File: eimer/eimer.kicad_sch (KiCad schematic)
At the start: 33 parts, among them J1 Conn_01x20, J2 Conn_01x20, J3 Conn_01x03, J4 USB_C_Receptacle_USB2.0_14P, SW1 SW_Push, U1 RP2040, U2 NCP1117-3.3_SOT223, U3 W25Q128JVS, Y1 12 MHz

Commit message: started layout of pcb
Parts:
- removed U2: NCP1117-3.3_SOT223, Package_TO_SOT_SMD:SOT-223-3_TabPin2, symbol Regulator_Linear:NCP1117-3.3_SOT223
- removed U3: W25Q128JVS, Package_SO:SOIC-8_5.3x5.3mm_P1.27mm, symbol Memory_Flash:W25Q128JVS
- added U2: MCP1700x-330xxTT, Package_TO_SOT_SMD:SOT-23, symbol Regulator_Linear:MCP1700x-330xxTT
- added U4: W25Q16JVUXIQ TR, Package_SON:Winbond_USON-8-1EP_3x2mm_P0.5mm_EP0.2x1.6mm, symbol Memory_Flash:W25Q16JVSS
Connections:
- net +3.3V: now also U2.2 (VO), U4.8 (VCC)
- net GND: now also U2.1 (GND), U4.4 (GND)
- net QSPI_SCLK: now also U4.6 (CLK)
- net QSPI_SD0: now also U4.5 (DI/IO_{0})
- net QSPI_SD1: now also U4.2 (DO/IO_{1})
- net QSPI_SD2: now also U4.3 (~{WP}/IO_{2})
- net QSPI_SD3: now also U4.7 (~{HOLD}/~{RESET}/IO_{3})
- net QSPI_SS: now also U4.1 (~{CS})
- net VBUS: now also U2.3 (VI)
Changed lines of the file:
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@@
 	)
 	(symbol
+		(lib_id "Memory_Flash:W25Q16JVSS")
+		(at 226.06 124.46 0)
+		(unit 1)
+		(body_style 1)
+		(exclude_from_sim no)
+		(in_bom yes)
+		(on_board yes)
+		(in_pos_files yes)
+		(dnp no)
+		(fields_autoplaced yes)
+		(property "Reference" "U4"
+			(at 237.49 123.1899 0)
+			(show_name no)
+			(do_not_autoplace no)
+			(effects
+				(font
+					(size 1.27 1.27)
+				)
+				(justify left)
+			)
+		)
+		(property "Value" "W25Q16JVUXIQ TR"
+			(at 237.49 125.7299 0)
+			(show_name no)
+			(do_not_autoplace no)
+			(effects
+				(font
+					(size 1.27 1.27)
+				)
+				(justify left)
+			)
+		)
+		(property "Footprint" "Package_SON:Winbond_USON-8-1EP_3x2mm_P0.5mm_EP0.2x1.6mm"
+			(at 226.06 124.46 0)
+			(hide yes)
+			(show_name no)
+			(do_not_autoplace no)
+			(effects
+				(font
+					(size 1.27 1.27)
+				)
+			)
+		)
+		(property "Datasheet" ""
+			(at 226.06 124.46 0)
+			(hide yes)
+			(show_name no)
+			(do_not_autoplace no)
+			(effects
+				(font
+					(size 1.27 1.27)
+				)
+			)
+		)
+		(property "Description" ""
+			(at 226.06 124.46 0)
+			(hide yes)
+			(show_name no)
+			(do_not_autoplace no)
+			(effects
+				(font
+					(size 1.27 1.27)
+				)
+			)
+		)
+		(pin "5"
+		)
+		(pin "8"
+		)
+		(pin "4"
+		)
+		(pin "3"
+		)
+		(pin "2"
+		)
+		(pin "6"
+		)
+		(pin "1"
+		)
+		(pin "7"
+		)
+		(instances
+			(project "eimer"
+				(path "/310aac61-9967-4677-964a-8a6056e13ca2"
+					(reference "U4")
+					(unit 1)
+				)
+			)
+		)
+	)
+	(symbol
 		(lib_id "Connector_Generic:Conn_01x20")
 		(at 55.88 87.63 0)
@@
 	)
 	(symbol
+		(lib_id "Regulator_Linear:MCP1700x-330xxTT")
+		(at 248.92 33.02 0)
+		(unit 1)
+		(body_style 1)
+		(exclude_from_sim no)
+		(in_bom yes)
+		(on_board yes)
+		(in_pos_files yes)
+		(dnp no)
+		(fields_autoplaced yes)
+		(property "Reference" "U2"
+			(at 248.92 26.67 0)
+			(show_name no)
+			(do_not_autoplace no)
+			(effects
+				(font
+					(size 1.27 1.27)
+				)
+			)
+		)
+		(property "Value" "MCP1700x-330xxTT"
+			(at 248.92 29.21 0)
+			(show_name no)
+			(do_not_autoplace no)
+			(effects
+				(font
+					(size 1.27 1.27)
+				)
+			)
+		)
+		(property "Footprint" "Package_TO_SOT_SMD:SOT-23"
+			(at 248.92 27.305 0)
+			(hide yes)
+			(show_name no)
+			(do_not_autoplace no)
+			(effects
+				(font
+					(size 1.27 1.27)
+				)
+			)
+		)
+		(property "Datasheet" "http://ww1.microchip.com/downloads/en/DeviceDoc/20001826D.pdf"
+			(at 248.92 33.02 0)
+			(hide yes)
+			(show_name no)
+			(do_not_autoplace no)
+			(effects
+				(font
+					(size 1.27 1.27)
+				)
+			)
+		)
+		(property "Description" "250mA Low Quiscent Current LDO, 3.3V output, SOT-23"
+			(at 248.92 33.02 0)
+			(hide yes)
+			(show_name no)
+			(do_not_autoplace no)
+			(effects
+				(font
+					(size 1.27 1.27)
+				)
+			)
+		)
+		(pin "3"
+		)
+		(pin "2"
+		)
+		(pin "1"
+		)
+		(instances
+			(project "eimer"
+				(path "/310aac61-9967-4677-964a-8a6056e13ca2"
+					(reference "U2")
+					(unit 1)
+				)
+			)
+		)
+	)
+	(symbol
 		(lib_id "Connector:USB_C_Receptacle_USB2.0_14P")
 		(at 194.31 48.26 0)
@@
 	)
 	(symbol
-		(lib_id "Regulator_Linear:NCP1117-3.3_SOT223")
-		(at 248.92 33.02 0)
-		(unit 1)
-		(body_style 1)
-		(exclude_from_sim no)
-		(in_bom yes)
-		(on_board yes)
-		(in_pos_files yes)
-		(dnp no)
-		(fields_autoplaced yes)
-		(property "Reference" "U2"
-			(at 248.92 26.67 0)
-			(show_name no)
-			(do_not_autoplace no)
-			(effects
-				(font
-					(size 1.27 1.27)
-				)
-			)
-		)
-		(property "Value" "NCP1117-3.3_SOT223"
-			(at 248.92 29.21 0)
-			(show_name no)
-			(do_not_autoplace no)
-			(effects
-				(font
-					(size 1.27 1.27)
-				)
-			)
-		)
-		(property "Footprint" "Package_TO_SOT_SMD:SOT-223-3_TabPin2"
-			(at 248.92 27.94 0)
-			(hide yes)
-			(show_name no)
-			(do_not_autoplace no)
-			(effects
-				(font
-					(size 1.27 1.27)
-				)
-			)
-		)
-		(property "Datasheet" "http://www.onsemi.com/pub_link/Collateral/NCP1117-D.PDF"
-			(at 251.46 39.37 0)
-			(hide yes)
-			(show_name no)
-			(do_not_autoplace no)
-			(effects
-				(font
-					(size 1.27 1.27)
-				)
-			)
-		)
-		(property "Description" "1A Low drop-out regulator, Fixed Output 3.3V, SOT-223"
-			(at 248.92 33.02 0)
-			(hide yes)
-			(show_name no)
-			(do_not_autoplace no)
-			(effects
-				(font
-					(size 1.27 1.27)
-				)
-			)
-		)
-		(pin "2"
-		)
-		(pin "3"
-		)
-		(pin "1"
-		)
-		(instances
-			(project "eimer"
-				(path "/310aac61-9967-4677-964a-8a6056e13ca2"
-					(reference "U2")
-					(unit 1)
-				)
-			)
-		)
-	)
-	(symbol
 		(lib_id "Device:C")
 		(at 43.18 34.29 0)
@@
 					(unit 1)
 				)
-			)
-		)
-	)
-	(symbol
-		(lib_id "Memory_Flash:W25Q128JVS")
-		(at 226.06 124.46 0)
-		(unit 1)
-		(body_style 1)
-		(exclude_from_sim no)
-		(in_bom yes)
-		(on_board yes)
-		(in_pos_files yes)
-		(dnp no)
-		(fields_autoplaced yes)
-		(property "Reference" "U3"
-			(at 237.49 123.1899 0)
-			(show_name no)
-			(do_not_autoplace no)
-			(effects
-				(font
-					(size 1.27 1.27)
-				)
-				(justify left)
-			)
-		)
-		(property "Value" "W25Q128JVS"
-			(at 237.49 125.7299 0)
-			(show_name no)
-			(do_not_autoplace no)
-			(effects
-				(font
-					(size 1.27 1.27)
-				)
-				(justify left)
-			)
-		)
-		(property "Footprint" "Package_SO:SOIC-8_5.3x5.3mm_P1.27mm"
-			(at 226.06 101.6 0)
-			(hide yes)
-			(show_name no)
-			(do_not_autoplace no)
-			(effects
-				(font
-					(size 1.27 1.27)
-				)
-			)
-		)
-		(property "Datasheet" "https://www.winbond.com/resource-files/w25q128jv_dtr%20revc%2003272018%20plus.pdf"
-			(at 226.06 99.06 0)
-			(hide yes)
-			(show_name no)
-			(do_not_autoplace no)
-			(effects
-				(font
-					(size 1.27 1.27)
-				)
-			)
-		)
-		(property "Description" "128Mbit / 16MiB Serial Flash Memory, Standard/Dual/Quad SPI, 2.7-3.6V, SOIC-8"
-			(at 226.06 96.52 0)
-			(hide yes)
-			(show_name no)
-			(do_not_autoplace no)
-			(effects
-				(font
-					(size 1.27 1.27)
-				)
-			)
-		)
-		(pin "1"
-		)
-		(pin "2"
-		)
-		(pin "8"
-		)
-		(pin "5"
-		)
-		(pin "7"
-		)
-		(pin "6"
-		)
-		(pin "3"
-		)
-		(pin "4"
-		)
-		(instances
-			(project "eimer"
-				(path "/310aac61-9967-4677-964a-8a6056e13ca2"
-					(reference "U3")
-					(unit 1)
-				)

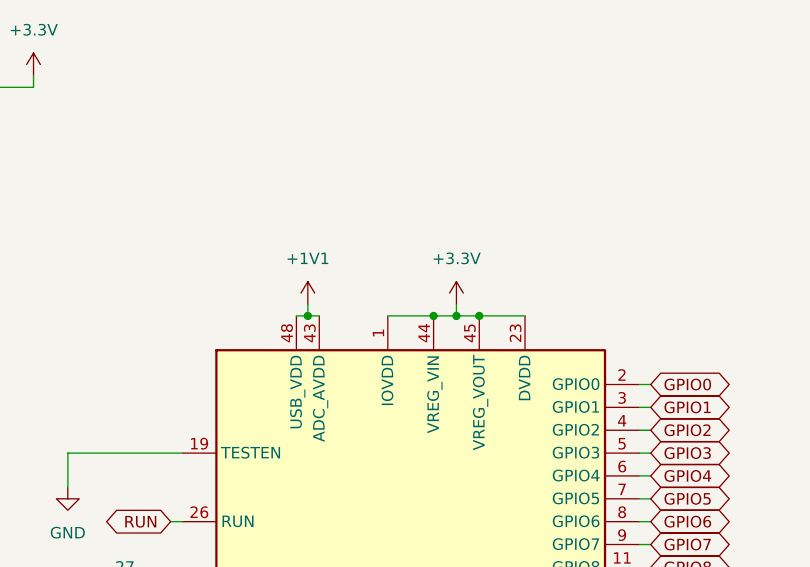
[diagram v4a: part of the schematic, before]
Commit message: fixed power nets
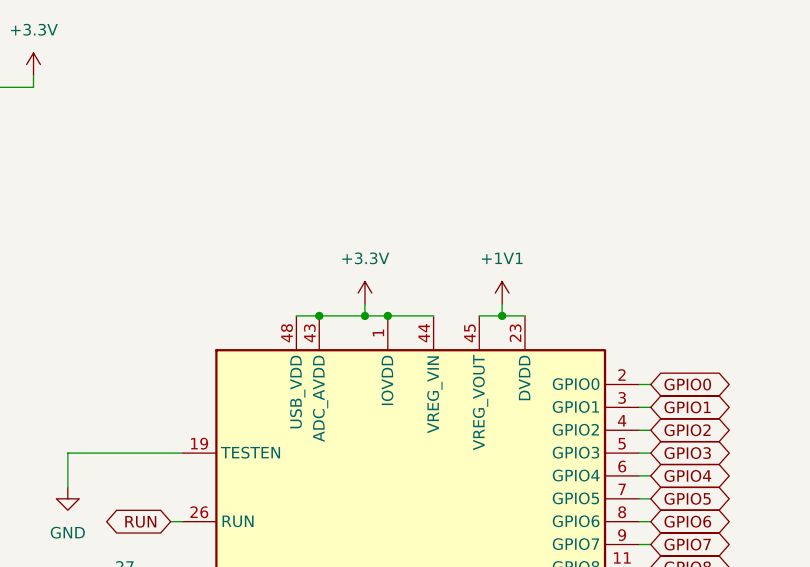
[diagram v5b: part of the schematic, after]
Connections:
- net +1V1: now also U1.23 (DVDD), U1.45 (VREG_VOUT), U1.50 (DVDD); no longer U1.43 (ADC_AVDD), U1.48 (USB_VDD)
- net +3.3V: now also U1.43 (ADC_AVDD), U1.48 (USB_VDD); no longer U1.23 (DVDD), U1.45 (VREG_VOUT), U1.50 (DVDD)
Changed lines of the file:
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@@
 	)
 	(junction
+		(at 120.65 100.33)
+		(diameter 0)
+		(color 0 0 0 0)
+	)
+	(junction
 		(at 110.49 30.48)
 		(diameter 0)
@@
 	)
 	(junction
-		(at 119.38 100.33)
-		(diameter 0)
-		(color 0 0 0 0)
-	)
-	(junction
 		(at 30.48 38.1)
 		(diameter 0)
@@
 	)
 	(junction
-		(at 138.43 100.33)
+		(at 123.19 30.48)
 		(diameter 0)
 		(color 0 0 0 0)
 	)
 	(junction
-		(at 123.19 30.48)
+		(at 85.09 38.1)
 		(diameter 0)
 		(color 0 0 0 0)
 	)
 	(junction
-		(at 85.09 38.1)
+		(at 97.79 30.48)
 		(diameter 0)
 		(color 0 0 0 0)
 	)
 	(junction
-		(at 97.79 30.48)
+		(at 140.97 100.33)
 		(diameter 0)
 		(color 0 0 0 0)
@@
 	)
 	(junction
-		(at 133.35 100.33)
+		(at 209.55 46.99)
 		(diameter 0)
 		(color 0 0 0 0)
 	)
 	(junction
-		(at 209.55 46.99)
+		(at 128.27 100.33)
 		(diameter 0)
 		(color 0 0 0 0)
@@
 	)
 	(junction
-		(at 226.06 109.22)
+		(at 125.73 100.33)
 		(diameter 0)
 		(color 0 0 0 0)
 	)
 	(junction
-		(at 135.89 100.33)
+		(at 226.06 109.22)
 		(diameter 0)
 		(color 0 0 0 0)
@@
 	(wire
 		(pts
-			(xy 133.35 100.33) (xy 135.89 100.33)
+			(xy 24.13 90.17) (xy 27.94 90.17)
 		)
 		(stroke
@@
 	(wire
 		(pts
-			(xy 24.13 90.17) (xy 27.94 90.17)
+			(xy 60.96 90.17) (xy 66.04 90.17)
 		)
 		(stroke
@@
 	(wire
 		(pts
-			(xy 60.96 90.17) (xy 66.04 90.17)
+			(xy 120.65 100.33) (xy 125.73 100.33)
 		)
 		(stroke
@@
 	(wire
 		(pts
-			(xy 118.11 100.33) (xy 119.38 100.33)
-		)
-		(stroke
-			(width 0)
-			(type default)
-		)
-	)
-	(wire
-		(pts
 			(xy 104.14 123.19) (xy 105.41 123.19)
 		)
@@
 	(wire
 		(pts
-			(xy 135.89 100.33) (xy 138.43 100.33)
-		)
-		(stroke
-			(width 0)
-			(type default)
-		)
-	)
-	(wire
-		(pts
 			(xy 156.21 184.15) (xy 157.48 184.15)
 		)
@@
 	(wire
 		(pts
+			(xy 140.97 99.06) (xy 140.97 100.33)
+		)
+		(stroke
+			(width 0)
+			(type default)
+		)
+	)
+	(wire
+		(pts
 			(xy 26.67 95.25) (xy 26.67 82.55)
 		)
@@
 	(wire
 		(pts
+			(xy 128.27 100.33) (xy 133.35 100.33)
+		)
+		(stroke
+			(width 0)
+			(type default)
+		)
+	)
+	(wire
+		(pts
 			(xy 233.68 40.64) (xy 248.92 40.64)
 		)
@@
 	(wire
 		(pts
+			(xy 125.73 99.06) (xy 125.73 100.33)
+		)
+		(stroke
+			(width 0)
+			(type default)
+		)
+	)
+	(wire
+		(pts
 			(xy 63.5 116.84) (xy 63.5 107.95)
 		)
@@
 	(wire
 		(pts
-			(xy 128.27 100.33) (xy 133.35 100.33)
-		)
-		(stroke
-			(width 0)
-			(type default)
-		)
-	)
-	(wire
-		(pts
-			(xy 119.38 100.33) (xy 120.65 100.33)
-		)
-		(stroke
-			(width 0)
-			(type default)
-		)
-	)
-	(wire
-		(pts
 			(xy 156.21 176.53) (xy 157.48 176.53)
 		)
@@
 	(wire
 		(pts
-			(xy 138.43 100.33) (xy 143.51 100.33)
-		)
-		(stroke
-			(width 0)
-			(type default)
-		)
-	)
-	(wire
-		(pts
 			(xy 201.93 114.3) (xy 201.93 116.84)
 		)
@@
 	(wire
 		(pts
-			(xy 135.89 99.06) (xy 135.89 100.33)
-		)
-		(stroke
-			(width 0)
-			(type default)
-		)
-	)
-	(wire
-		(pts
 			(xy 156.21 125.73) (xy 157.48 125.73)
 		)
@@
 	(wire
 		(pts
-			(xy 148.59 38.1) (xy 161.29 38.1)
+			(xy 140.97 100.33) (xy 143.51 100.33)
 		)
 		(stroke
@@
 	(wire
 		(pts
-			(xy 110.49 38.1) (xy 123.19 38.1)
+			(xy 148.59 38.1) (xy 161.29 38.1)
 		)
 		(stroke
@@
 	(wire
 		(pts
-			(xy 198.12 116.84) (xy 201.93 116.84)
+			(xy 110.49 38.1) (xy 123.19 38.1)
 		)
 		(stroke
@@
 	(wire
 		(pts
-			(xy 156.21 143.51) (xy 157.48 143.51)
+			(xy 198.12 116.84) (xy 201.93 116.84)
 		)
 		(stroke
@@
 	(wire
 		(pts
-			(xy 24.13 105.41) (xy 27.94 105.41)
+			(xy 156.21 143.51) (xy 157.48 143.51)
 		)
 		(stroke
@@
 	(wire
 		(pts
-			(xy 148.59 30.48) (xy 161.29 30.48)
+			(xy 24.13 105.41) (xy 27.94 105.41)
 		)
 		(stroke
@@
 	(wire
 		(pts
-			(xy 119.38 99.06) (xy 119.38 100.33)
+			(xy 148.59 30.48) (xy 161.29 30.48)
 		)
 		(stroke
@@
 	(wire
 		(pts
+			(xy 138.43 100.33) (xy 140.97 100.33)
+		)
+		(stroke
+			(width 0)
+			(type default)
+		)
+	)
+	(wire
+		(pts
 			(xy 256.54 33.02) (xy 262.89 33.02)
 		)
@@
 	(wire
 		(pts
+			(xy 125.73 100.33) (xy 128.27 100.33)
+		)
+		(stroke
+			(width 0)
+			(type default)
+		)
+	)
+	(wire
+		(pts
+			(xy 118.11 100.33) (xy 120.65 100.33)
+		)
+		(stroke
+			(width 0)
+			(type default)
+		)
+	)
+	(wire
+		(pts
 			(xy 40.64 121.92) (xy 41.91 121.92)
 		)
@@
 	(symbol
 		(lib_id "power:+3.3V")
-		(at 135.89 99.06 0)
+		(at 125.73 99.06 0)
 		(unit 1)
 		(body_style 1)
@@
 		(fields_autoplaced yes)
 		(property "Reference" "#PWR02"
-			(at 135.89 102.87 0)
+			(at 125.73 102.87 0)
 			(hide yes)
 			(show_name no)
@@
 		)
 		(property "Value" "+3.3V"
-			(at 135.89 93.98 0)
+			(at 125.73 93.98 0)
 			(show_name no)
 			(do_not_autoplace no)
@@
 		)
 		(property "Footprint" ""
-			(at 135.89 99.06 0)
+			(at 125.73 99.06 0)
 			(hide yes)
 			(show_name no)
@@
 		)
 		(property "Datasheet" ""
-			(at 135.89 99.06 0)
+			(at 125.73 99.06 0)
 			(hide yes)
 			(show_name no)
@@
 		)
 		(property "Description" "Power symbol creates a global label with name \"+3.3V\""
-			(at 135.89 99.06 0)
+			(at 125.73 99.06 0)
 			(hide yes)
 			(show_name no)
@@
 	(symbol
 		(lib_id "power:+1V1")
-		(at 119.38 99.06 0)
+		(at 140.97 99.06 0)
 		(unit 1)
 		(body_style 1)
@@
 		(fields_autoplaced yes)
 		(property "Reference" "#PWR01"
-			(at 119.38 102.87 0)
+			(at 140.97 102.87 0)
 			(hide yes)
 			(show_name no)
@@
 		)
 		(property "Value" "+1V1"
-			(at 119.38 93.98 0)
+			(at 140.97 93.98 0)
 			(show_name no)
 			(do_not_autoplace no)
@@
 		)
 		(property "Footprint" ""
-			(at 119.38 99.06 0)
+			(at 140.97 99.06 0)
 			(hide yes)
 			(show_name no)
@@
 		)
 		(property "Datasheet" ""
-			(at 119.38 99.06 0)
+			(at 140.97 99.06 0)
 			(hide yes)
 			(show_name no)
@@
 		)
 		(property "Description" "Power symbol creates a global label with name \"+1V1\""
-			(at 119.38 99.06 0)
+			(at 140.97 99.06 0)
 			(hide yes)
 			(show_name no)
